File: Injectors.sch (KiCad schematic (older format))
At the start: 36 parts, among them Q1 VND14NV04, Q2 VND14NV04, Q3 VND14NV04, Q4 VND14NV04, Q5 VND14NV04, Q6 VND14NV04

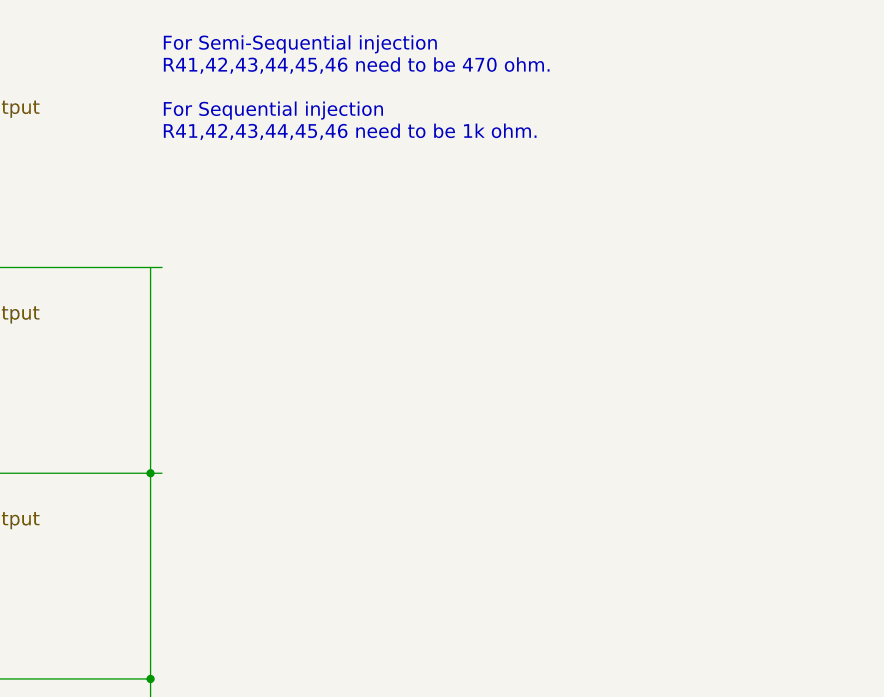
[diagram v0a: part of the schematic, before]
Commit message: Updated Schematics, PDF, BOM for 4cyl Sequential Injection
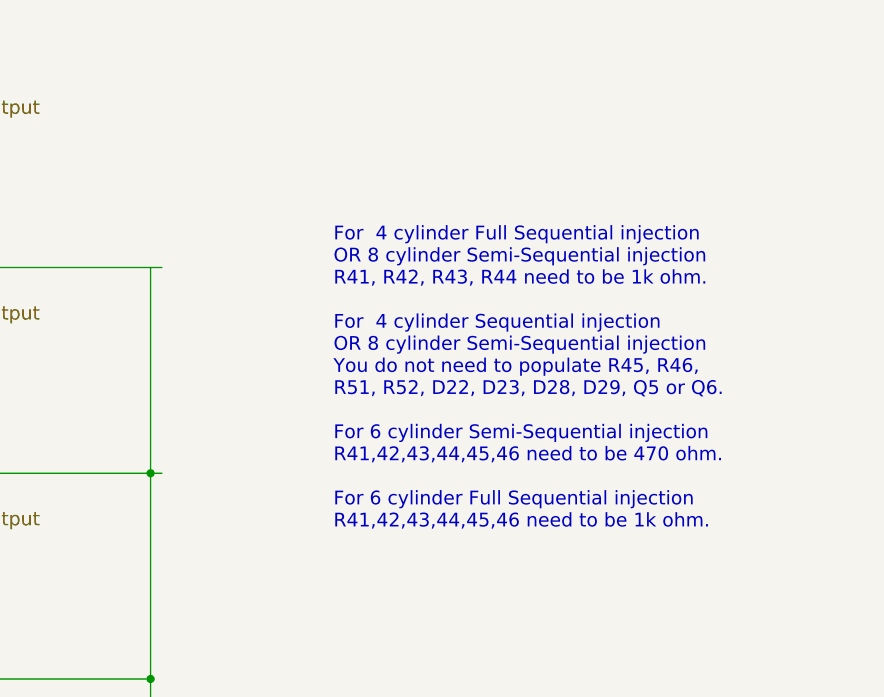
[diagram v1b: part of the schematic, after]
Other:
- note added: "For 4 cylinder Full Sequential injection\nOR 8 cylinder Semi-Sequential injection \nR41, R42, R43, R44 need to be 1k ohm.\n\nFor 4 cylinder Sequential injection\nOR 8 cylinder Semi-Sequential injection\nYou do not need to populate R45, R46, \nR51, R52, D22, D23, D28, D29, Q5 or Q6.\n\nFor 6 cylinder Semi-Sequential injection\nR41,42,43,44,45,46 need to be 470 ohm.\n\nFor 6 cylinder Full Sequentia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"
- note removed: "For Semi-Sequential injection\nR41,42,43,44,45,46 need to be 470 ohm.\n\nFor Sequential injection \nR41,42,43,44,45,46 need to be 1k ohm."
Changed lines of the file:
@@
-EESchema Schematic File Version 2  date Tue 24 Jan 2012 02:18:15 PM EST
+EESchema Schematic File Version 2  date Tue 24 Jan 2012 11:15:10 PM EST
 LIBS:power
 LIBS:device
@@
 Sheet 6 7
 Title "Jaguar PCB for FreeEMS"
-Date "24 jan 2012"
+Date "25 jan 2012"
 Rev "A.1"
 Comp "diyefi.org"
@@
 Comment4 ""
 $EndDescr
-Text Notes 5450 1400 0    60   ~ 0
-For Semi-Sequential injection\nR41,42,43,44,45,46 need to be 470 ohm.\n\nFor Sequential injection \nR41,42,43,44,45,46 need to be 1k ohm.
+Text Notes 6200 3100 0    60   ~ 0
+For  4 cylinder Full Sequential injection\nOR 8 cylinder Semi-Sequential injection \nR41, R42, R43, R44 need to be 1k ohm.\n\nFor  4 cylinder Sequential injection\nOR 8 cylinder Semi-Sequential injection\nYou do not need to populate R45, R46, \nR51, R52, D22, D23, D28, D29, Q5 or Q6.\n\nFor 6 cylinder Semi-Sequential injection\nR41,42,43,44,45,46 need to be 470 ohm.\n\nFor 6 cylinder Full Sequential injection \nR41,42,43,44,45,46 need to be 1k ohm.
 Text HLabel 2400 5950 0    60   Input ~ 0
 Injector6

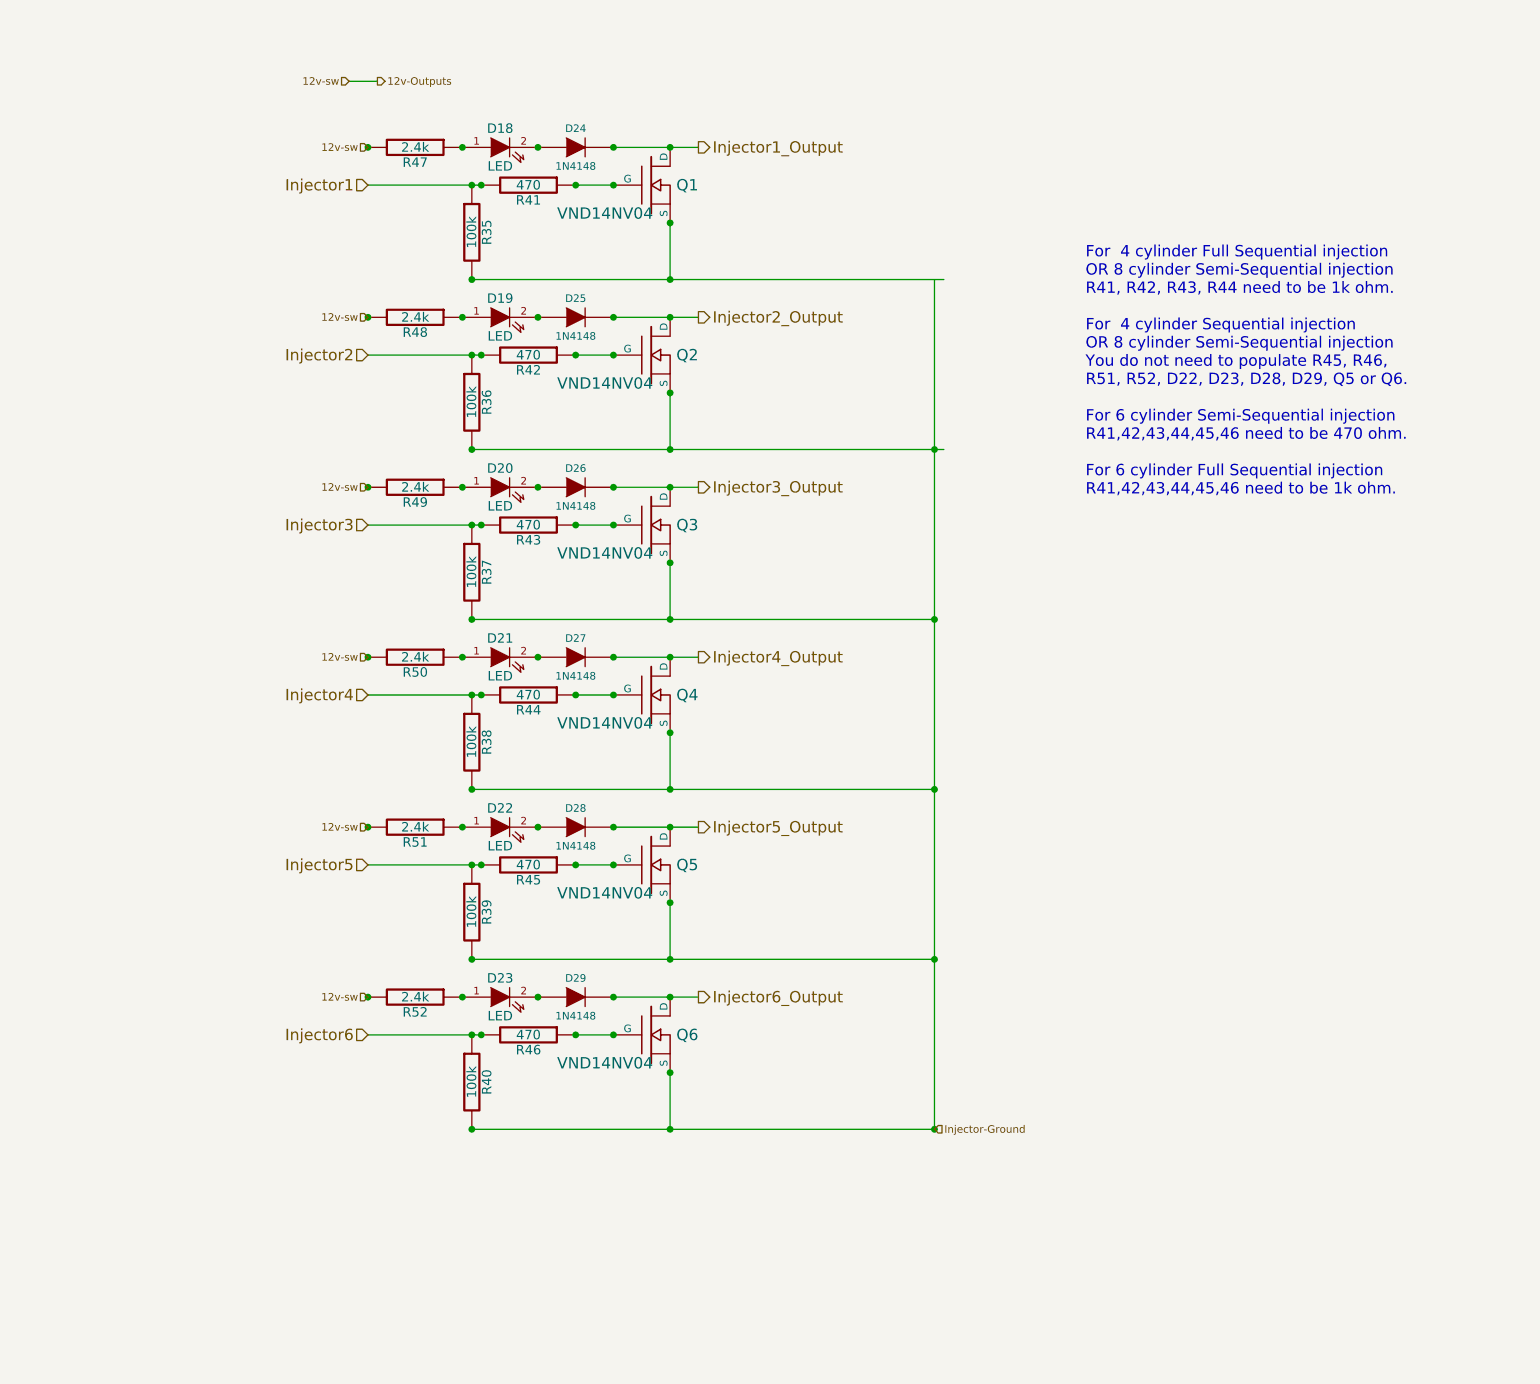
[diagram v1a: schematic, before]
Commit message: Updated everything for up to 8 cylinder engines
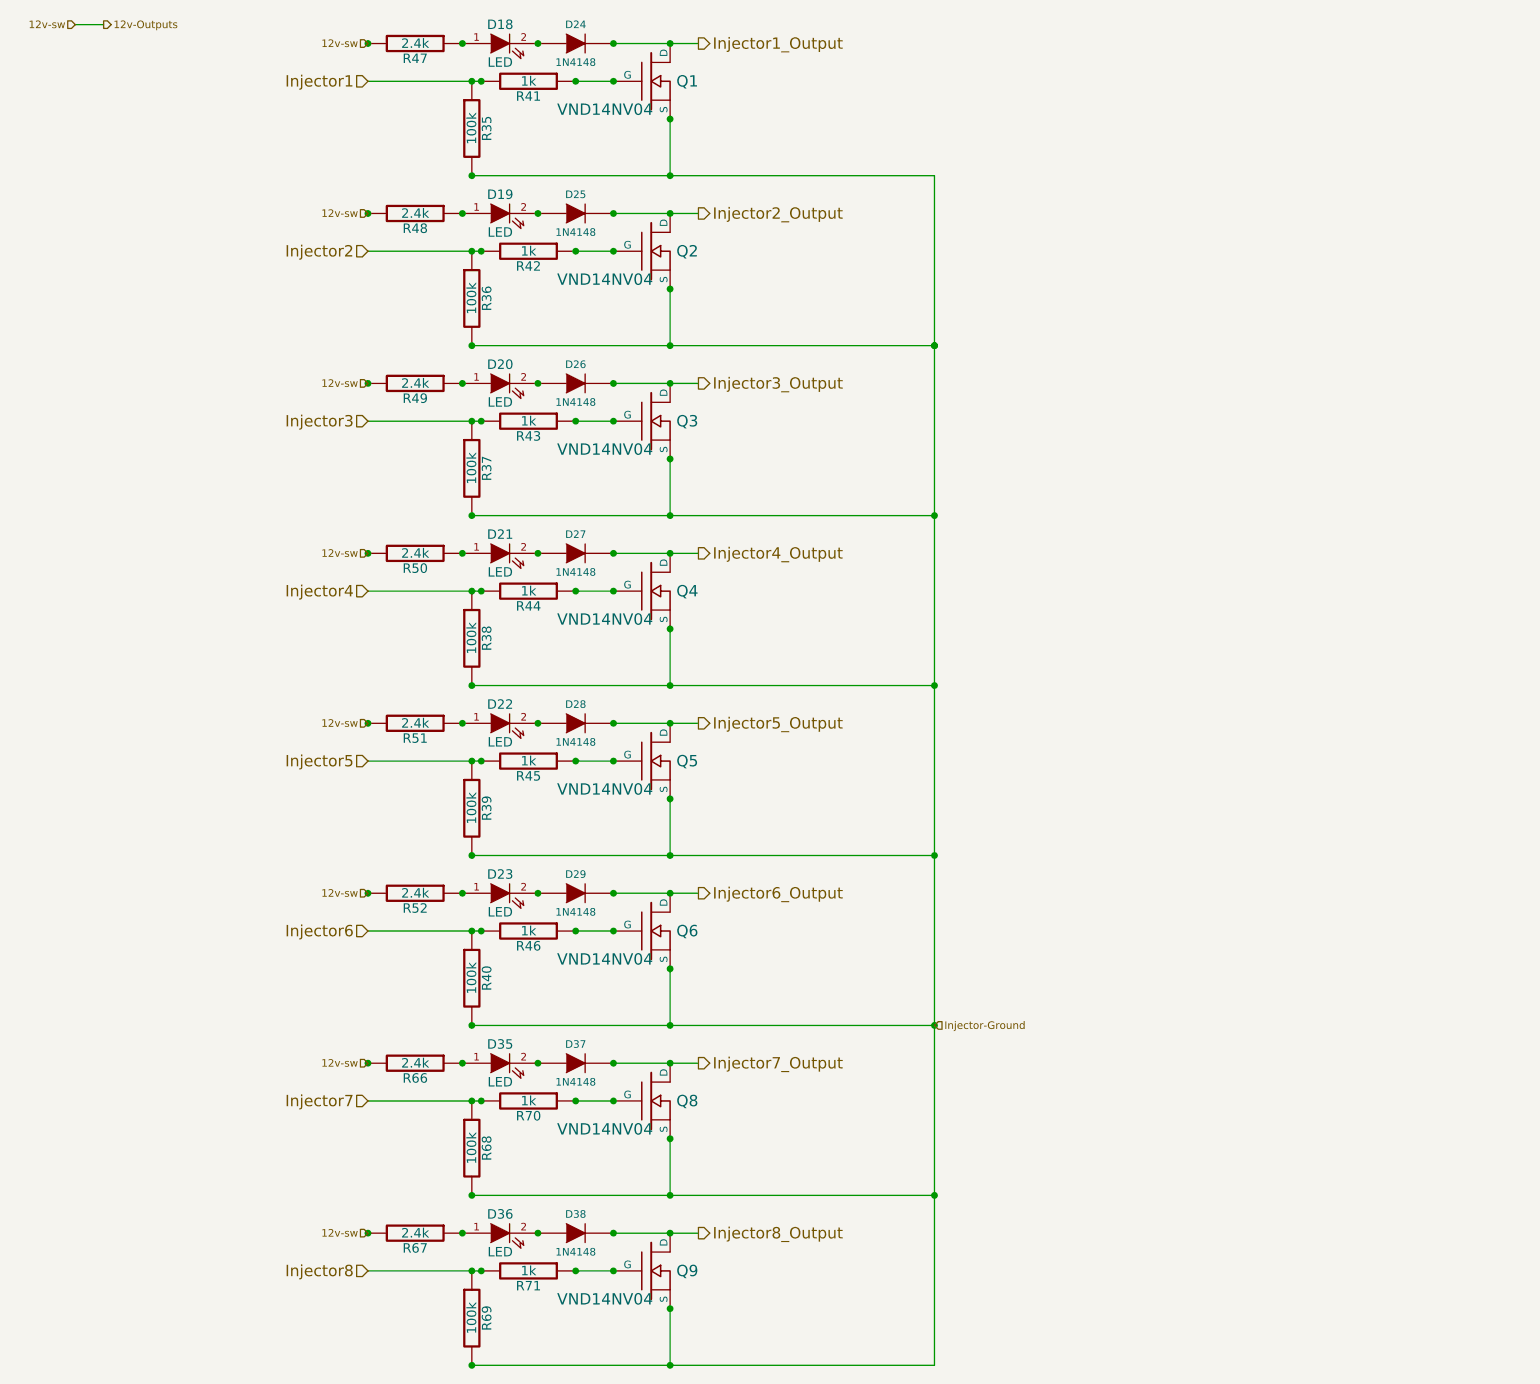
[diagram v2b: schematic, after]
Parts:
- added D35, D36: LED, symbol LED
- added D37, D38: 1N4148, symbol DIODE
- added Q8, Q9: VND14NV04, symbol MOSFET_N
- added R66, R67: 2.4k, symbol R
- added R68, R69: 100k, symbol R
- added R70, R71: 1k, symbol R
- R41, R42, R43, R44, R45, R46: value 470 -> 1k; Digikey (none) -> 1.00KXBK-ND
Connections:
- net labels added: Injector7, Injector7_Output, Injector8, Injector8_Output
- wire segments 32 -> 42
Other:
- note removed: "For 4 cylinder Full Sequential injection\nOR 8 cylinder Semi-Sequential injection \nR41, R42, R43, R44 need to be 1k ohm.\n\nFor 4 cylinder Sequential injection\nOR 8 cylinder Semi-Sequential injection\nYou do not need to populate R45, R46, \nR51, R52, D22, D23, D28, D29, Q5 or Q6.\n\nFor 6 cylinder Semi-Sequential injection\nR41,42,43,44,45,46 need to be 470 ohm.\n\nFor 6 cylinder Full Sequentia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"
- moved on the sheet: D18, D19, D20, D21, D22, D23, D24, D25, D26, D27, D28, D29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

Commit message: modified:   Outputs.sch
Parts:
- renumbered Q8 to Q7, Q9 to Q8
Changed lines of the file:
@@
-EESchema Schematic File Version 2  date Thu 26 Jan 2012 03:16:21 AM EST
+EESchema Schematic File Version 2  date Thu 26 Jan 2012 12:42:01 PM EST
 LIBS:power
 LIBS:device
@@
 $EndComp
 $Comp
-L MOSFET_N Q9
+L MOSFET_N Q8
 U 1 1 4F20C5E0
 P 3900 7200
-F 0 "Q9" H 4150 7200 60  0000 R CNN
+F 0 "Q8" H 4150 7200 60  0000 R CNN
 F 1 "VND14NV04" H 3910 7050 60  0000 R CNN
 	1    3900 7200
@@
 Injector7_Output
 $Comp
-L MOSFET_N Q8
+L MOSFET_N Q7
 U 1 1 4F20C5D8
 P 3900 6300
-F 0 "Q8" H 4150 6300 60  0000 R CNN
+F 0 "Q7" H 4150 6300 60  0000 R CNN
 F 1 "VND14NV04" H 3910 6150 60  0000 R CNN
 	1    3900 6300
